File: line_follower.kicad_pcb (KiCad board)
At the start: 2 copper layers, 151.1 x 176.3 mm, 101 parts, among them J1 Conn_01x20_Socket, J10 Conn_01x20_Pin, J11 Conn_01x20_Pin, J12 Conn_01x02_Socket, J13 Conn_01x04_Pin, J2 Conn_01x20_Socket, J3 Conn_01x06_Socket, J4 Conn_01x06_Socket, J5 XT60-M, J6 Conn_01x02_Socket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

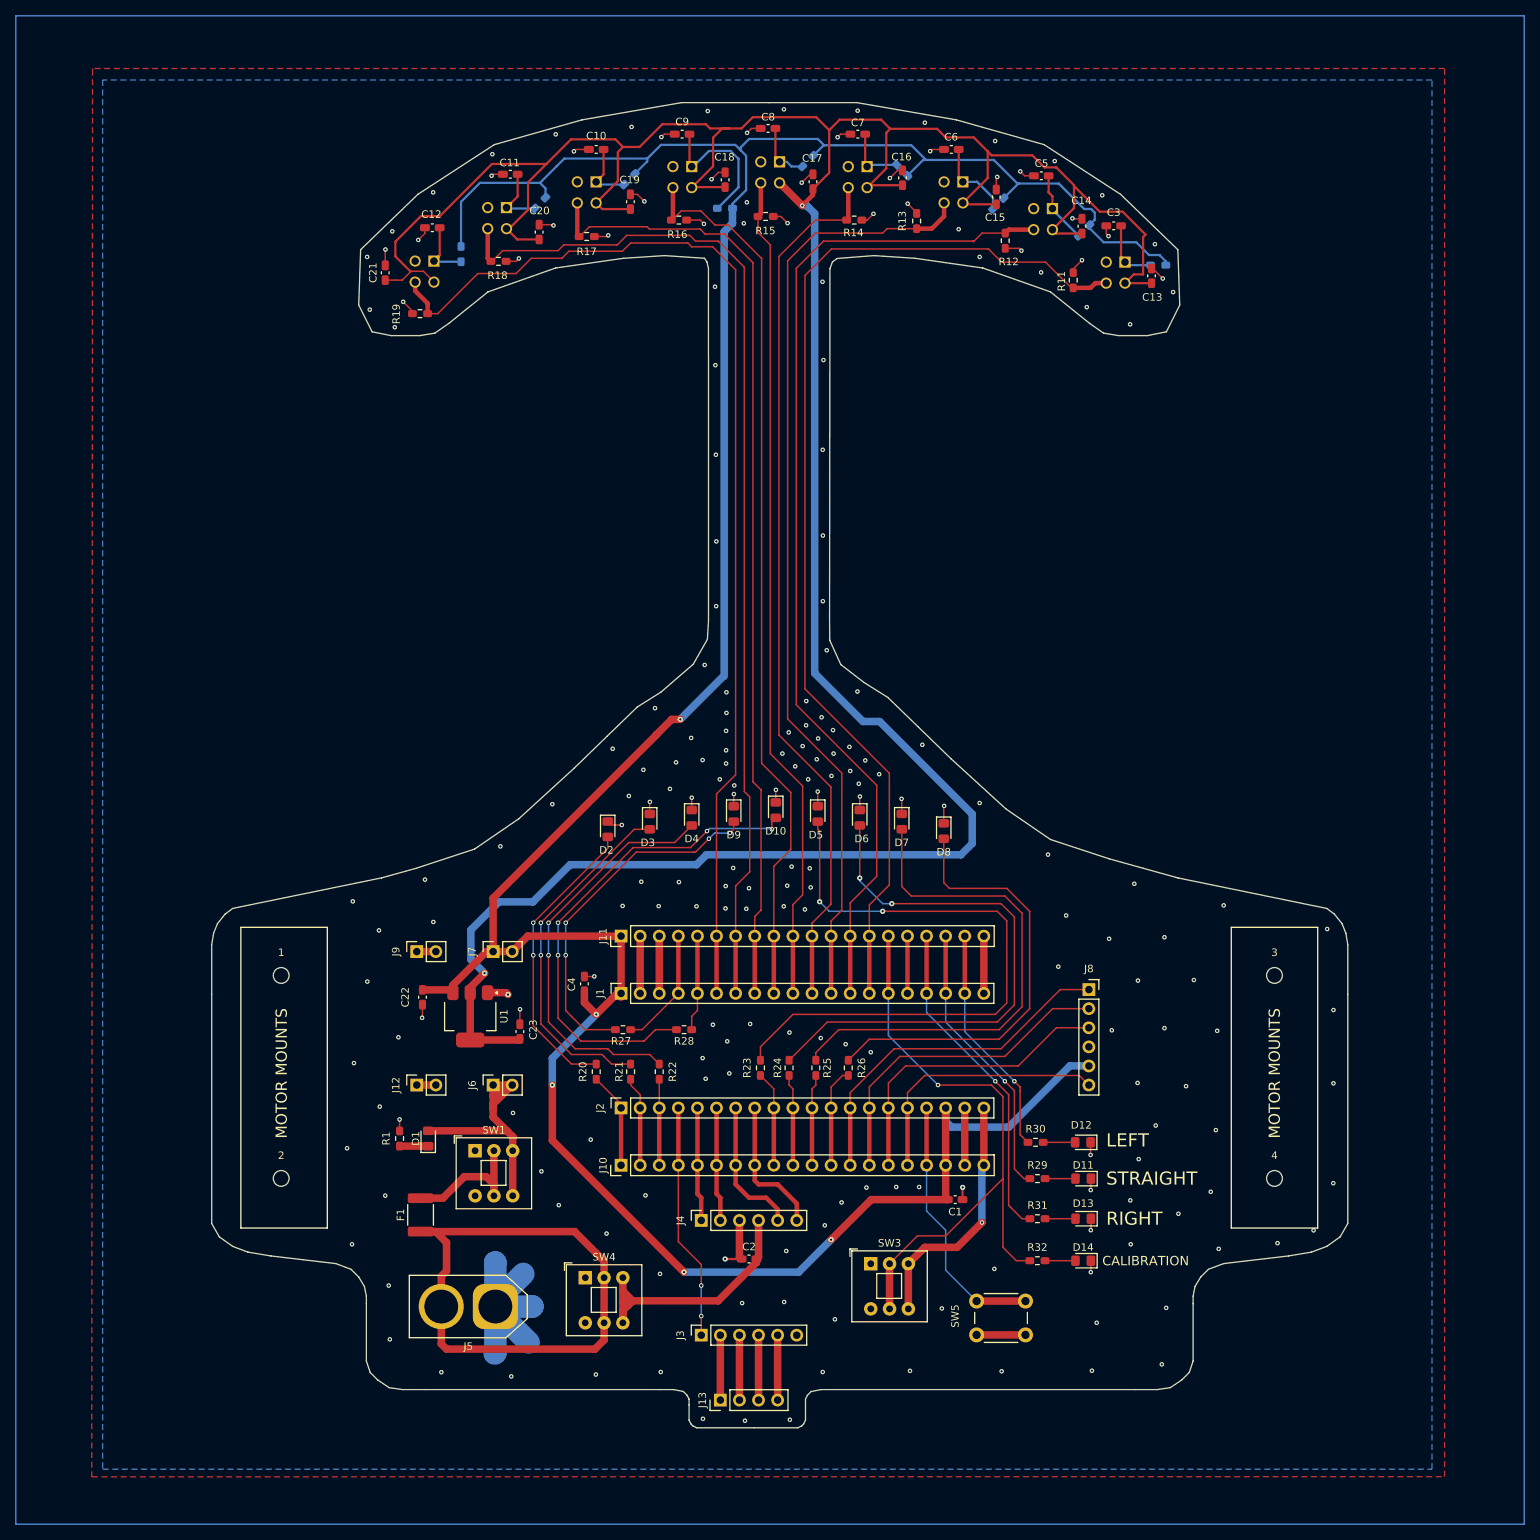
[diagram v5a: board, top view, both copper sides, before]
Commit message: battery mount holes placed, pcb complete
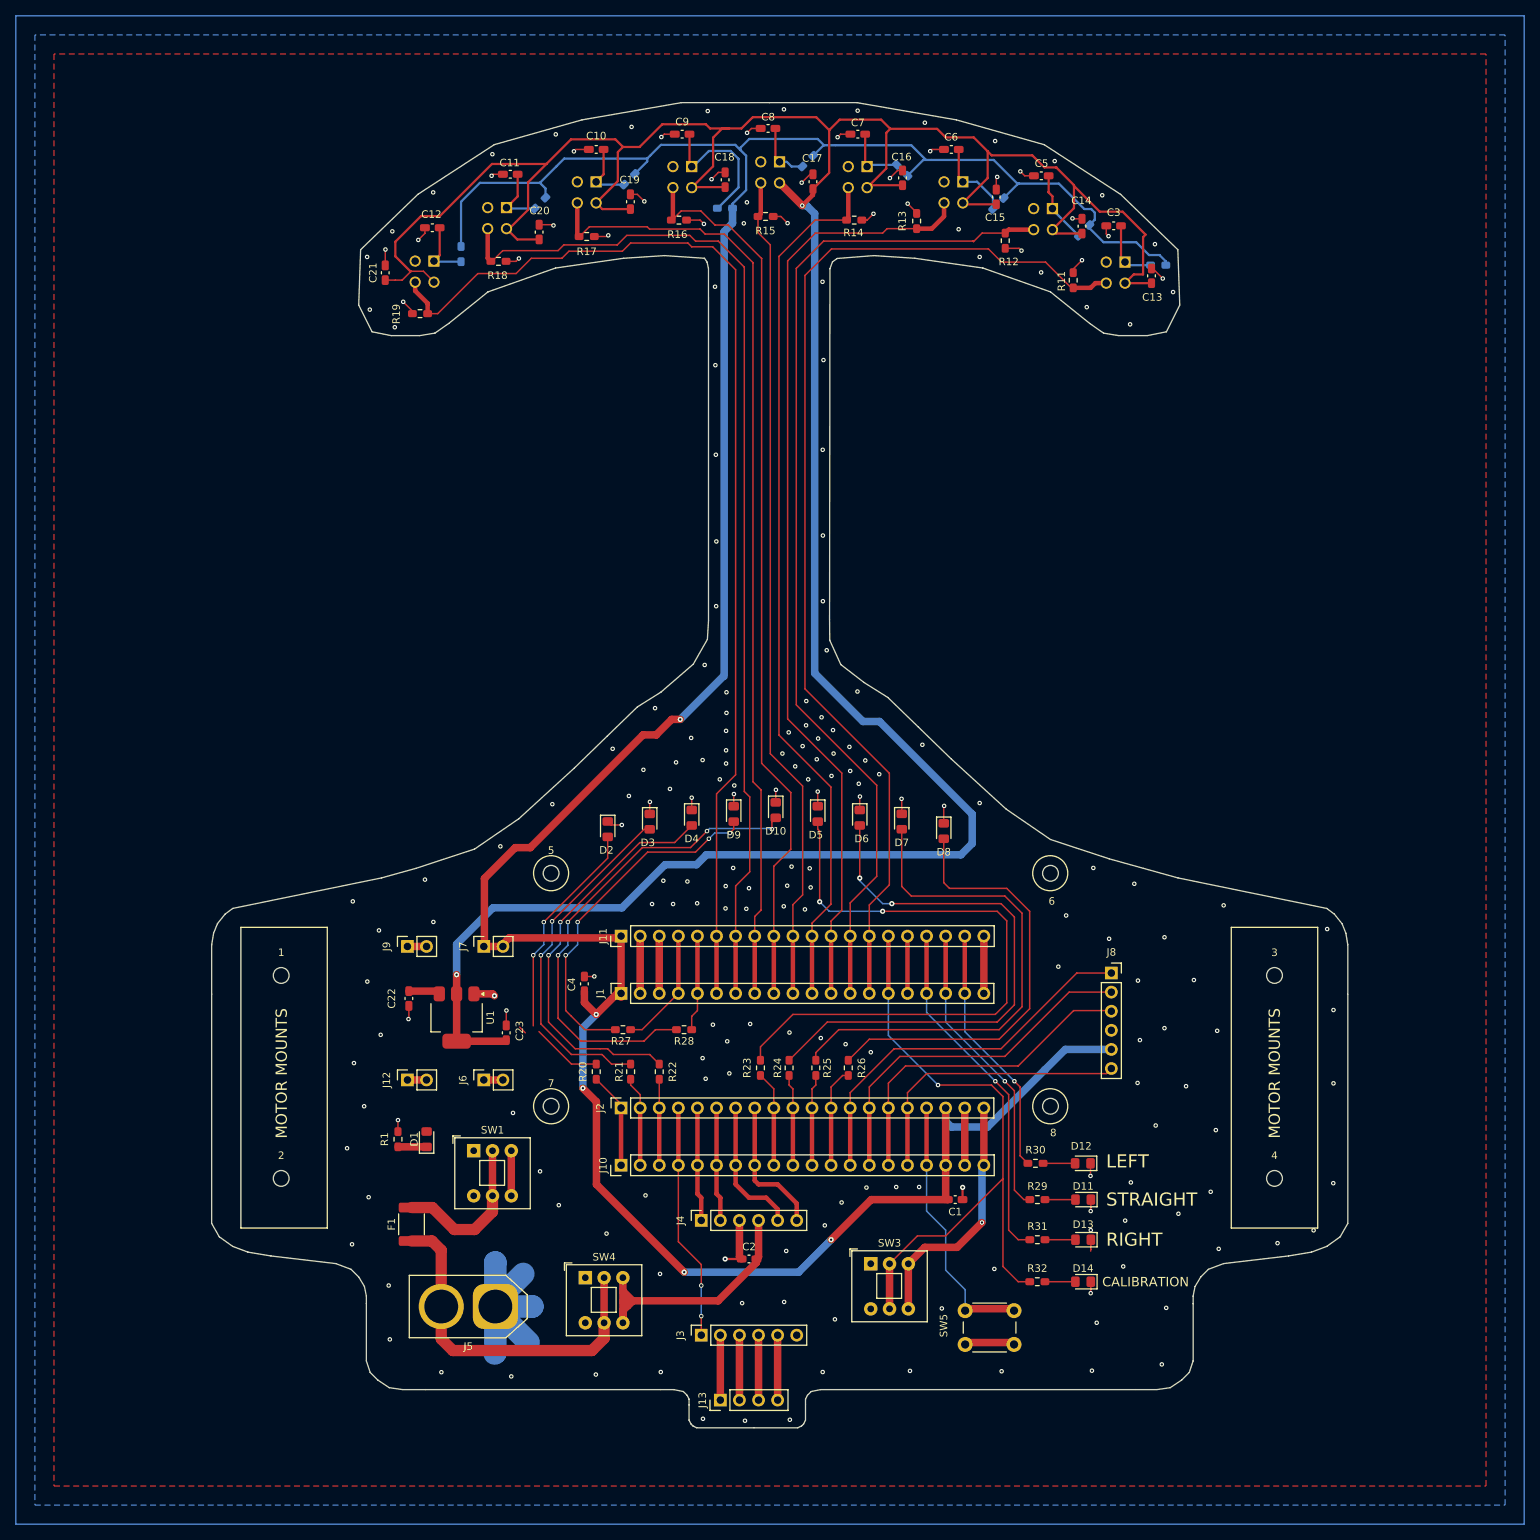
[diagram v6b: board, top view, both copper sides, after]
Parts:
- added 5: MountingHole_2.1mm, MountingHole:MountingHole_2.1mm, F.Cu at (106.8, 167.4)
- added 6: MountingHole_2.1mm, MountingHole:MountingHole_2.1mm, F.Cu at (173.2, 167.4)
- added 7: MountingHole_2.1mm, MountingHole:MountingHole_2.1mm, F.Cu at (106.8, 198.4)
- added 8: MountingHole_2.1mm, MountingHole:MountingHole_2.1mm, F.Cu at (173.2, 198.4)
- moved J8 3.71 mm to (181.3, 180.7)
- moved D12 2.79 mm to (177.5, 206.0)
- moved R30 2.79 mm to (171.2, 206.0)
- moved D11 2.79 mm to (177.5, 210.8)
- moved D13 2.79 mm to (177.5, 216.2)
- moved D14 2.79 mm to (177.5, 221.7)
- moved R29 2.79 mm to (171.5, 210.8)
- moved R31 2.79 mm to (171.5, 216.2)
- moved R32 2.79 mm to (171.5, 221.7)
- moved SW5 1.98 mm to (168.3, 230.1)
- moved C22 1.82 mm to (87.8, 184.1)
- moved C23 1.82 mm to (100.8, 188.6)
- moved U1 1.82 mm to (94.2, 186.6)
- moved F1 1.74 mm to (88.2, 214.1)
- moved J12 1.41 mm to (87.7, 194.9)
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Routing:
- net BAT+: track 76.8 -> 47.3 mm
- net /BUCK_IN: track 37.3 -> 7.83 mm
- net /5V_STM: track 414.5 -> 410.0 mm
- net /PB7: track 40.6 -> 44.6 mm
- net /PB6: track 43.9 -> 47.8 mm
- net /PB5: track 47.1 -> 51.0 mm
- net /FUSE_OUT : track 17.4 -> 21.1 mm
- net /PC15: track 43.9 -> 47.0 mm
- net /EN: track 35.3 -> 38.1 mm
- net /LEFT: track 30.9 -> 33.7 mm
- net /PC14: track 37.4 -> 40.1 mm
- net /CALIB: track 82.0 -> 84.6 mm
- net Net-(D4-A): track 54.7 -> 53.8 mm
- net Net-(D9-A): track 47.9 -> 47.1 mm
- net Net-(D3-A): track 47.2 -> 46.5 mm
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
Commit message: added logo
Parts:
- added G***: LOGO, Robo Logo:robo_logo.pretty, F.Cu at (135.8, 113.3)
- moved C2 2.24 mm to (131.1, 217.7)
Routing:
- net /PA6: track 119.9 -> 52.7 mm
- net /VCC_DRV: track 37.4 -> 46.7 mm
- net /EEP: track 31.5 -> 34.3 mm
- net GND: track 151.2 -> 150.3 mm

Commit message: final pcb
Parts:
- added R33: 10k, Resistor_SMD:R_0603_1608Metric_Pad0.98x0.95mm_HandSolder, F.Cu at (174.4, 226.8)
- added R34: 10k, Resistor_SMD:R_0603_1608Metric_Pad0.98x0.95mm_HandSolder, F.Cu at (149.6, 230.9)
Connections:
- SW5 pad 1: GND -> /3.3V_STM_1
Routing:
- net /PA6: track 52.7 -> 119.9 mm
- net /BUCK_IN: track 7.83 -> 28.2 mm
- net /3.3V_STM_1: track 33.4 -> 49.6 mm
- net /5V_STM: track 410.0 -> 420.3 mm
- net /CALIB: track 84.6 -> 90.6 mm
- net /PB9: track 35.6 -> 41.1 mm
- net Net-(D10-A): track 65.0 -> 66.7 mm
- net GND: track 150.3 -> 148.8 mm, vias 219 -> 221
